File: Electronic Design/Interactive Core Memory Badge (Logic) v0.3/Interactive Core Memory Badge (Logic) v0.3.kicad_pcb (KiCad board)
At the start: 2 copper layers, 85.2 x 170.1 mm, 124 parts, among them J1 SSW-116-22-F-S-VS‎, J10 Conn_01x08_Female, J11 Conn_01x08_Female, J12 Conn_01x08_Female, J13 Conn_01x08_Female, J14 Conn_01x08_Female, J2 SSW-116-22-F-S-VS‎, J3 BM03B-PASS-1-TFT__LF__SN_, J4 Conn_01x02_Male, J5 SSW-104-22-L-S-VS, J6 Conn_01x08_Female, J7 Conn_01x04_Male, J8 Conn_01x08_Female, J9 TSM-106-03-T-DV‎, Q1 IRLML6344TRPBF, Q10 MMBT4401LT1G, Q11 MMBT4403LT1G, Q12 MMBT4401LT1G, Q13 MMBT4403LT1G, Q14 MMBT4401LT1G, Q15 MMBT4403LT1G, Q16 MMBT4401LT1G, Q17 MMBT4403LT1G, Q18 MMBT4401LT1G, Q19 MMBT4403LT1G, Q2 MMBT4403LT1G, Q20 MMBT4401LT1G, Q21 MMBT4403LT1G, Q22 MMBT4401LT1G, Q3 MMBT4401LT1G, Q4 MMBT4401LT1G, Q5 MMBT4403LT1G, Q6 MMBT4401LT1G, Q7 MMBT4403LT1G, Q8 MMBT4401LT1G, Q9 MMBT4403LT1G, SW1 JS102011SAQN, U1 LD1117S33TR_SOT223, U10 M24C01-RMN, U2 Teensy-LC, U3 LM393, U4 74HC02, U5 MCP23017_SO, U6 MCP23017_SO, U7 SN74LV1T125DBVR, U8 74AC04, U9 74AC04, X1 SAO_conn_SFH11-NBPC-D03-ST-BK, X2 SAO_conn_SFH11-NBPC-D03-ST-BK

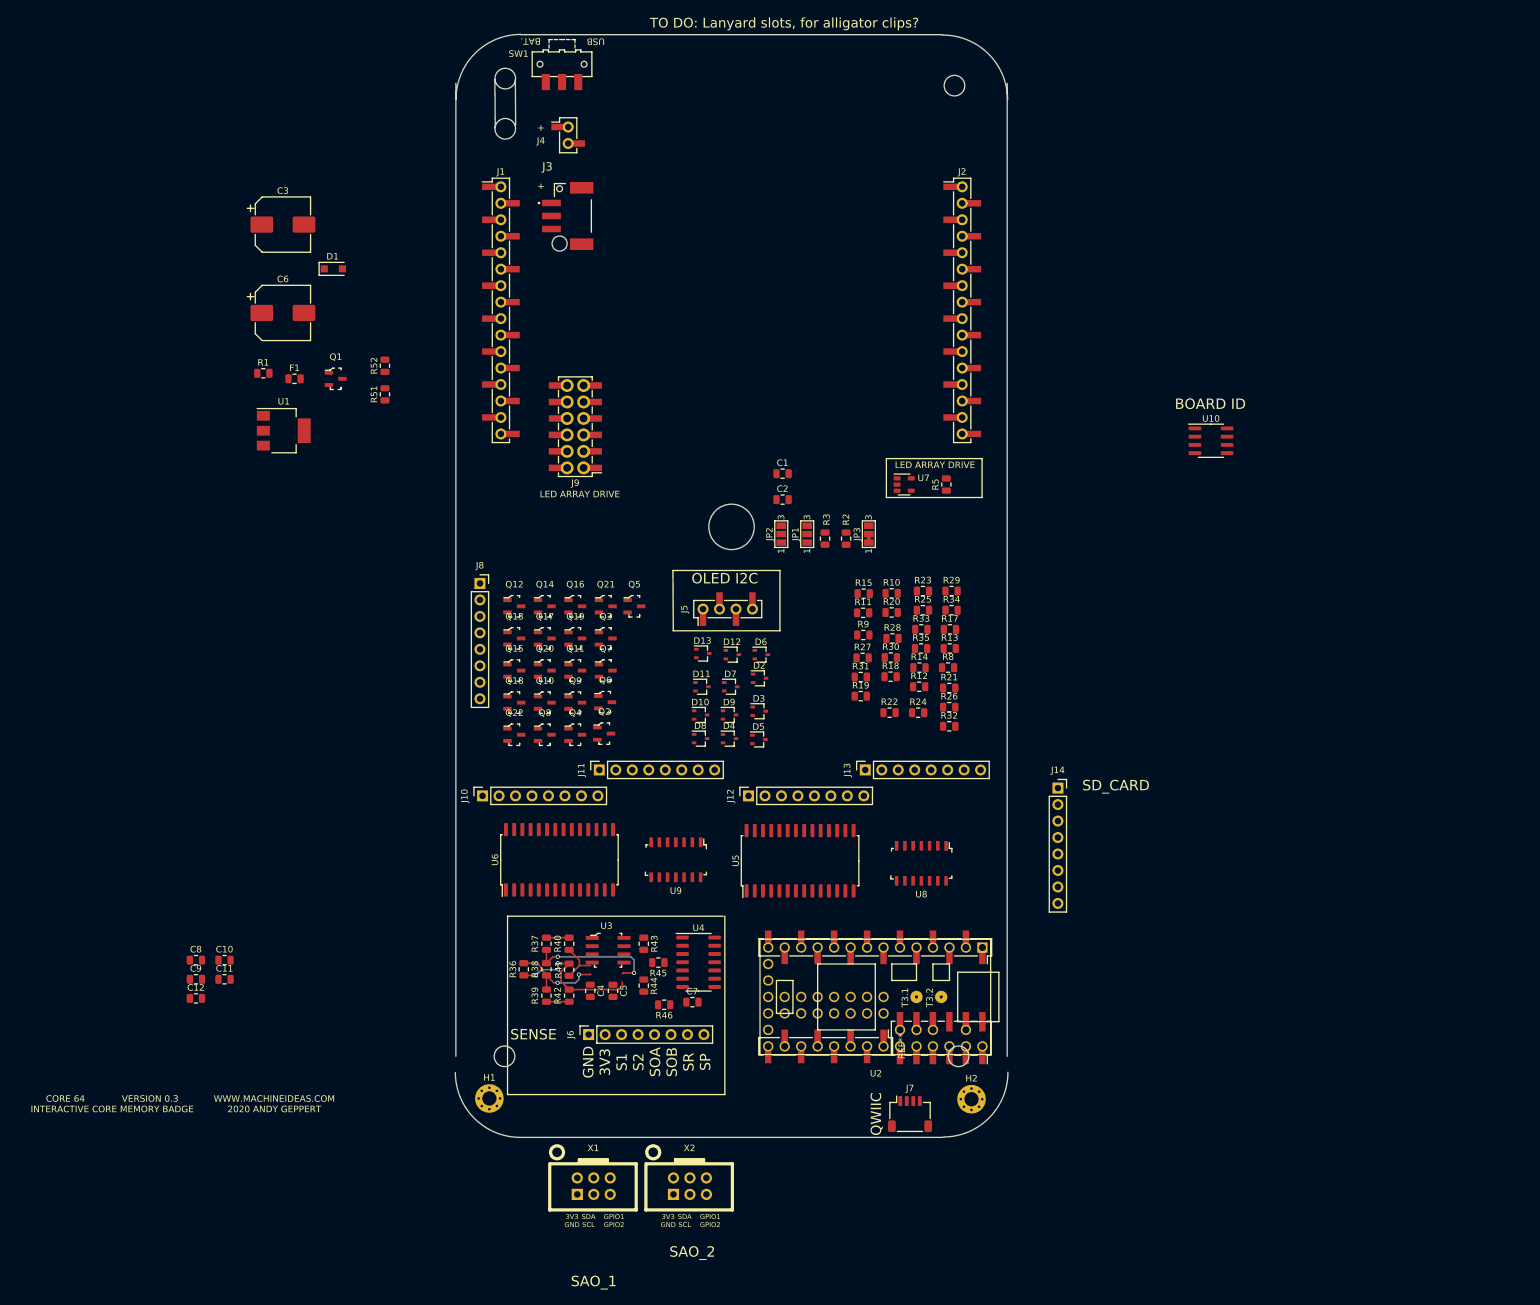
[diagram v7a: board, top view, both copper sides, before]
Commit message: Logic board layout power routing
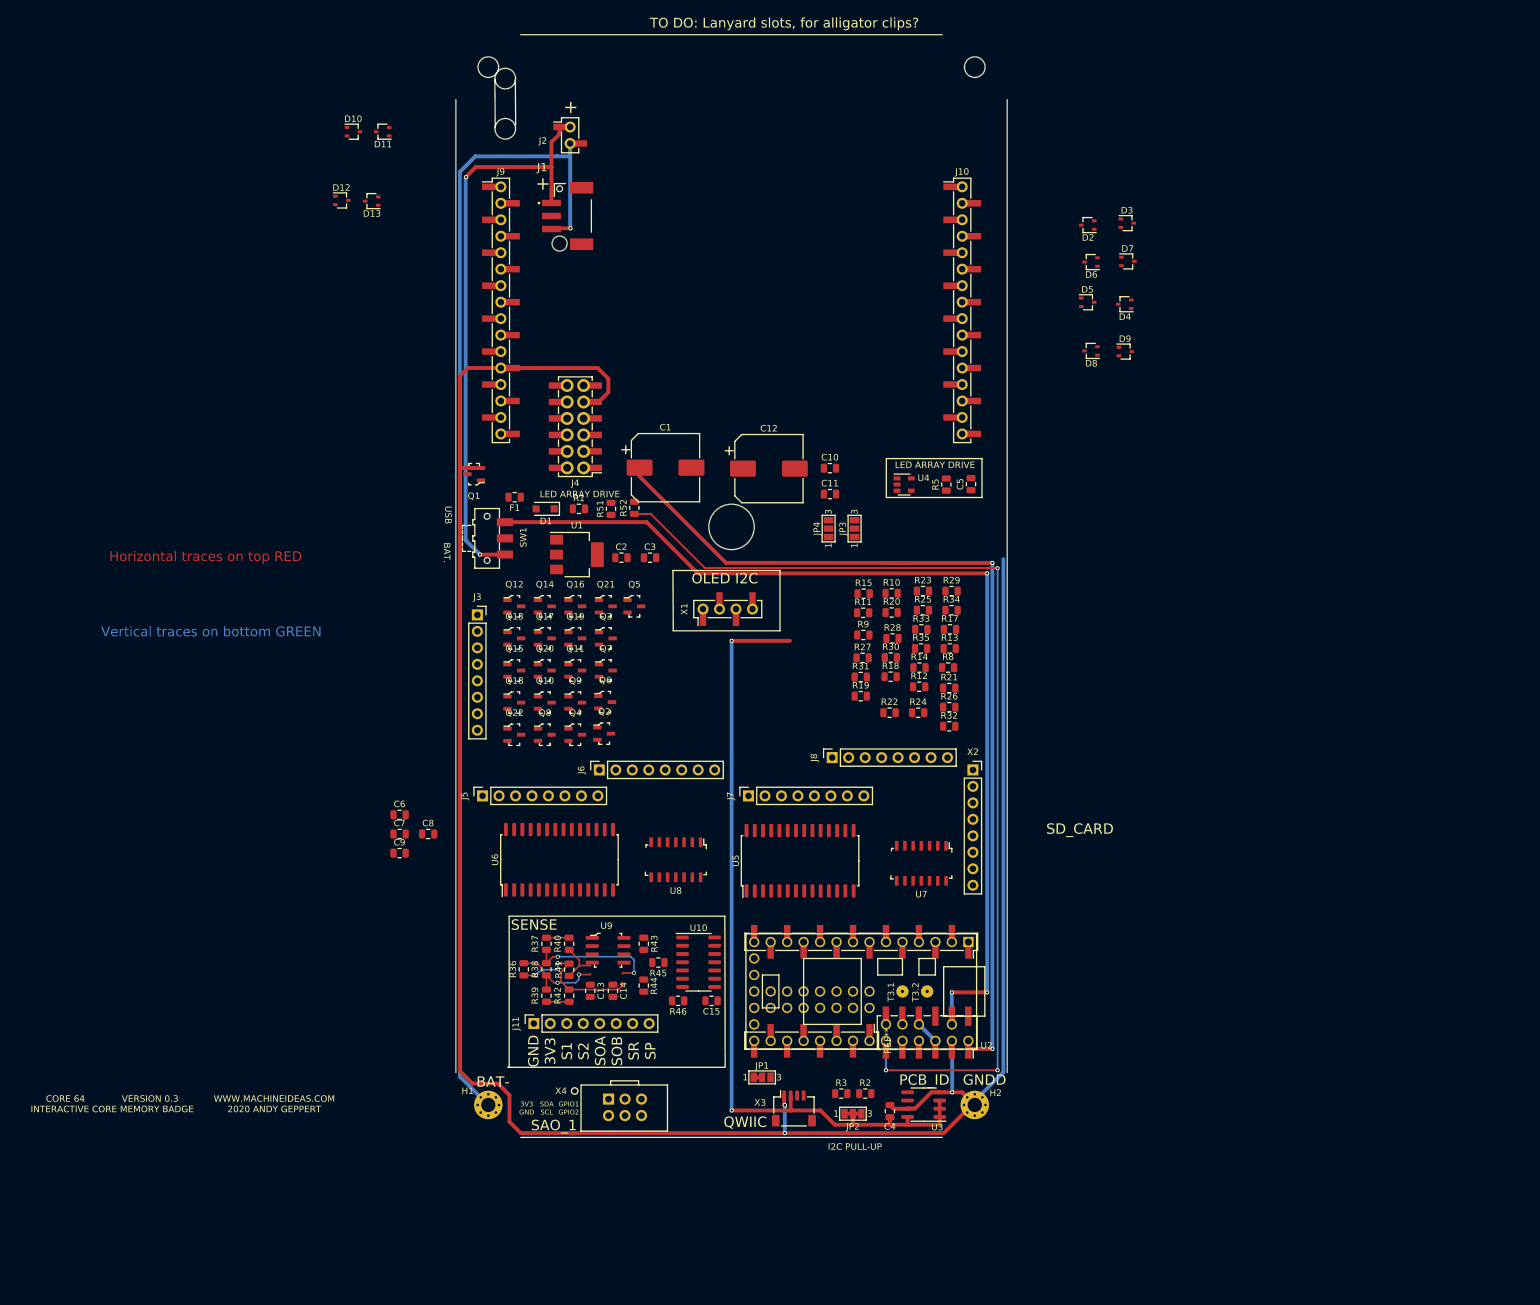
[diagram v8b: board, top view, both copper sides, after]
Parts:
- removed the C10 at (-78.2, 100.2)
- removed the C6 at (-69.2, 0.40)
- removed J14: Conn_01x08_Female, Connector_PinSocket_2.54mm:PinSocket_1x08_P2.54mm_Vertical
- removed the JP3 at (21.2, 34.5)
- removed the U10 at (73.9, 20.1)
- removed the X1 at (-21.3, 135.0)
- added C1: 1000uF, Capacitor_SMD:CP_Elec_10x10, F.Cu at (-10.2, 24.2)
- added C12: 1000uF, Capacitor_SMD:CP_Elec_10x10, F.Cu at (5.76, 24.4)
- added C2: 0.1uF, Capacitor_SMD:C_0805_2012Metric, F.Cu at (-17.0, 38.1)
- added C4: 0.1uF, Capacitor_SMD:C_0805_2012Metric, F.Cu at (24.4, 123.5)
- added C5: 0.1uF, Capacitor_SMD:C_0805_2012Metric, F.Cu at (36.9, 26.8)
- added JP1: SolderJumper_3_Bridged12, Jumper:SolderJumper-3_P1.3mm_Bridged12_Pad1.0x1.5mm_NumberLabels, F.Cu at (4.71, 118.2)
- added JP2: SolderJumper_3_Bridged123, Jumper:SolderJumper-3_P1.3mm_Bridged123_Pad1.0x1.5mm_NumberLabels, F.Cu at (18.7, 123.8)
- added U3: M24C01-RMN, Package_SO:SOIC-8_3.9x4.9mm_P1.27mm, F.Cu at (29.6, 122.5)
- added X4: SAO_conn_SFH11-NBPC-D03-ST-BK, badgelife_sao_v169bis:Badgelife-SAOv169-BADGE-2x3, F.Cu at (-16.5, 122.8)
- C3: value 1000uF -> 10uF; footprint Capacitor_SMD:CP_Elec_8x10 -> Capacitor_SMD:C_0805_2012Metric
- H1: value GND PAD -> -BATT PAD
- X2: value SAO_conn_SFH11-NBPC-D03-ST-BK -> Conn_01x08_Female; footprint badgelife_sao_v169bis:Badgelife-SAOv169-BADGE-2x3 -> Connector_PinSocket_2.54mm:PinSocket_1x08_P2.54mm_Vertical
- moved D10 104.6 mm to (-58.3, -27.6)
- moved D11 98.7 mm to (-53.8, -27.6), turned to 180 degrees
- moved D3 94.3 mm to (61.0, -13.4)
- moved D12 92.4 mm to (-60.1, -16.9)
- moved D4 90.5 mm to (60.6, -0.95), turned to 180 degrees
- moved D7 89.7 mm to (61.1, -7.55)
- moved D13 86.4 mm to (-55.5, -16.9), turned to 180 degrees
- moved D2 86.3 mm to (54.9, -13.2), turned to 180 degrees
- moved R2 85.6 mm to (20.6, 120.8), turned to 0 degrees
- moved R3 85.6 mm to (16.9, 120.8), turned to 0 degrees
- moved D8 84.8 mm to (55.4, 6.25), turned to 180 degrees
- moved D5 84.3 mm to (54.9, -1.25)
- moved D9 82.8 mm to (60.7, 6.35)
- moved D6 79.0 mm to (55.4, -7.45), turned to 180 degrees
- moved X2 77.6 mm to (37.2, 70.8)
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- renumbered C1 to C10, C2 to C11, C4 to C13, C5 to C14, C7 to C15, C8 to C6, C9 to C7, C11 to C8, C12 to C9, J3 to J1, J2 to J10, J6 to J11, J4 to J2, J8 to J3, J9 to J4, J10 to J5, J11 to J6, J12 to J7, J13 to J8, J1 to J9, JP1 to JP3, JP2 to JP4, U4 to U10, U7 to U4, U8 to U7, U9 to U8, U3 to U9, J5 to X1, J7 to X3
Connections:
- C3 pad 1: CUR_LOW -> 3V3_800mA
- H2 pad 1: -BATT -> TEENSY_GND
- J10 pad 13: CUR_LOW -> +VSW
- J3 pad 4: CUR_LOW -> +VSW
- J3 pad 5: CUR_LOW -> +VSW
- J4 pad 2: CUR_LOW -> +VSW
- Q1 pad 1: CUR_LOW -> +VSW
- R1 pad 2: CUR_LOW -> +VSW
- R2 pad 2: I2C_DATA -> I2C_CLOCK
- R3 pad 2: I2C_CLOCK -> I2C_DATA
- R51 pad 1: CUR_LOW -> +VSW
- U1 pad 3: CUR_LOW -> +VSW
- U2 pad 20: SD_CLK -> Net-(JP1-Pad1)
- U2 pad 21: SD_CD -> Net-(JP1-Pad3)
- U2 pad 22: Net-(U2-Pad22) -> SD_CD
- U2 pad 33: CUR_LOW -> +VSW
- U4 pad 5: CUR_LOW -> +VSW
- X2 pad 1: 3V3_800mA -> SD_CD
- X2 pad 2: TEENSY_GND -> SD_CS
- X2 pad 3: I2C_DATA -> SD_DI
- X2 pad 4: I2C_CLOCK -> SD_DO
- X2 pad 5: SAO2_GPIO1(TX) -> SD_CLK
- X2 pad 6: SAO2_GPIO2(RX) -> TEENSY_GND
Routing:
- net TEENSY_GND: track 3.50 -> 344.0 mm, vias 0 -> 4
- net -BATT: track 0.00 -> 181.4 mm, vias 0 -> 1
- net VSW_HALF_VOL_MONITOR: track 0.00 -> 158.6 mm, vias 0 -> 3
- net 5V_USB: track 0.00 -> 152.6 mm, vias 0 -> 3
- net +VSW: track 0.00 -> 139.9 mm, vias 0 -> 2
- net 3V3_800mA: track 3.50 -> 128.0 mm, vias 0 -> 2
- net +BATT: track 0.00 -> 90.7 mm, vias 0 -> 2
- net TEENSY_3V3: track 0.00 -> 3.59 mm
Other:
- board size 85.2 x 170.1 mm -> 85 x 170 mm
- net class Core Current: trace_width 0.635 -> 0.6; via_dia 0.635 -> 0.65; via_drill 0.4 -> 0.35
- net class Core Current 20mil removed
- net class Default: trace_width 0.254 -> 0.6; via_dia 0.635 -> 0.65; via_drill 0.4 -> 0.35
- net class Signal added: clearance 0.127, trace_width 0.4, via_dia 0.65, via_drill 0.35
- board text added: "BAT-"
- board text added: "GNDD"
- board text added: "Horizontal traces on top RED"
- board text added: "I2C PULL-UP"
- board text added: "PCB_ID"
- board text added: "Vertical traces on bottom GREEN"
- board text removed: "BOARD ID"
- board text removed: "SAO_2"
